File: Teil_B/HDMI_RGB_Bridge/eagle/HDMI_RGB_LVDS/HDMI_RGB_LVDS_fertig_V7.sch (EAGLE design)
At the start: 95 parts, among them CON1 KLDX-0202-A-LT, CON2 FCI-10029449-111RLF, CON3 XF2M-4015-1A, CON4 FCI-10033526-N3212LF, CON5 MOLEX-53261-0671, CON6 FI-X30SSLA-HF, IC2 WPMDL1300331BD, IC4 AT24C01C-SSHM-B, IC5 TFP401APZP, IC6 ATMEGA88PA, IC7 FT232RL, IC8 SN75LVDS83BDGGR, Q1 ATS073ASM-1, T1 IRLML5203TRPBF, T2 IRLML2502TRPBF

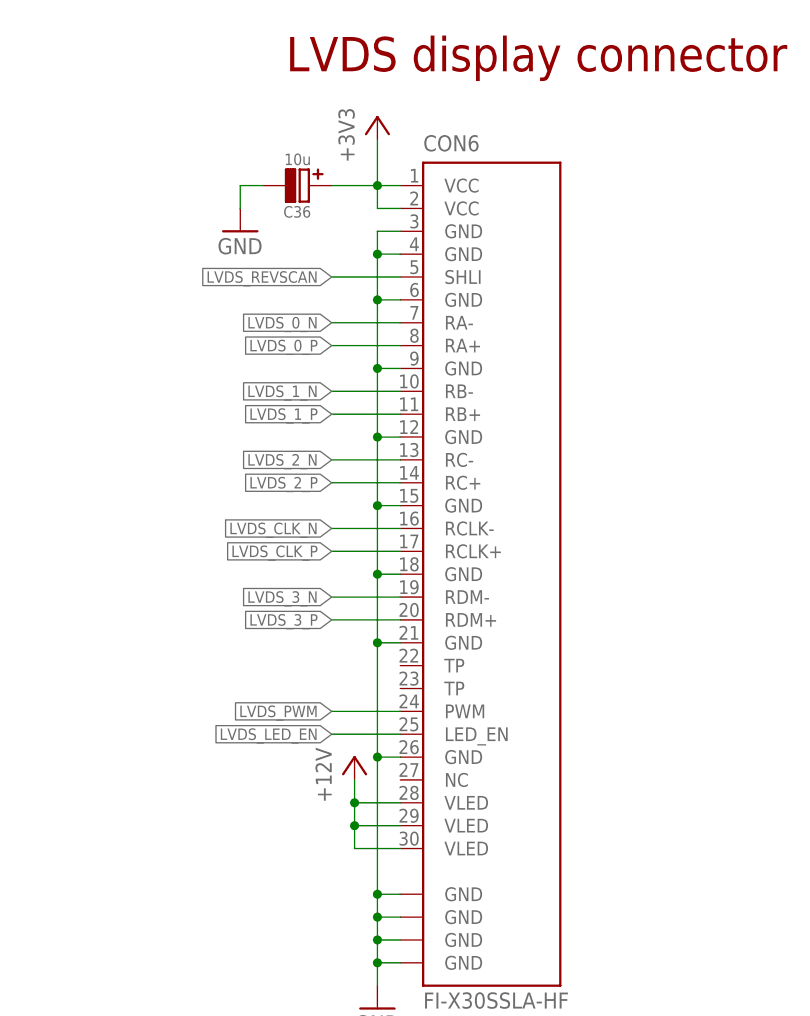
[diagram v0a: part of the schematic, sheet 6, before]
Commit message: reviewd lbr, changd schematics to V7
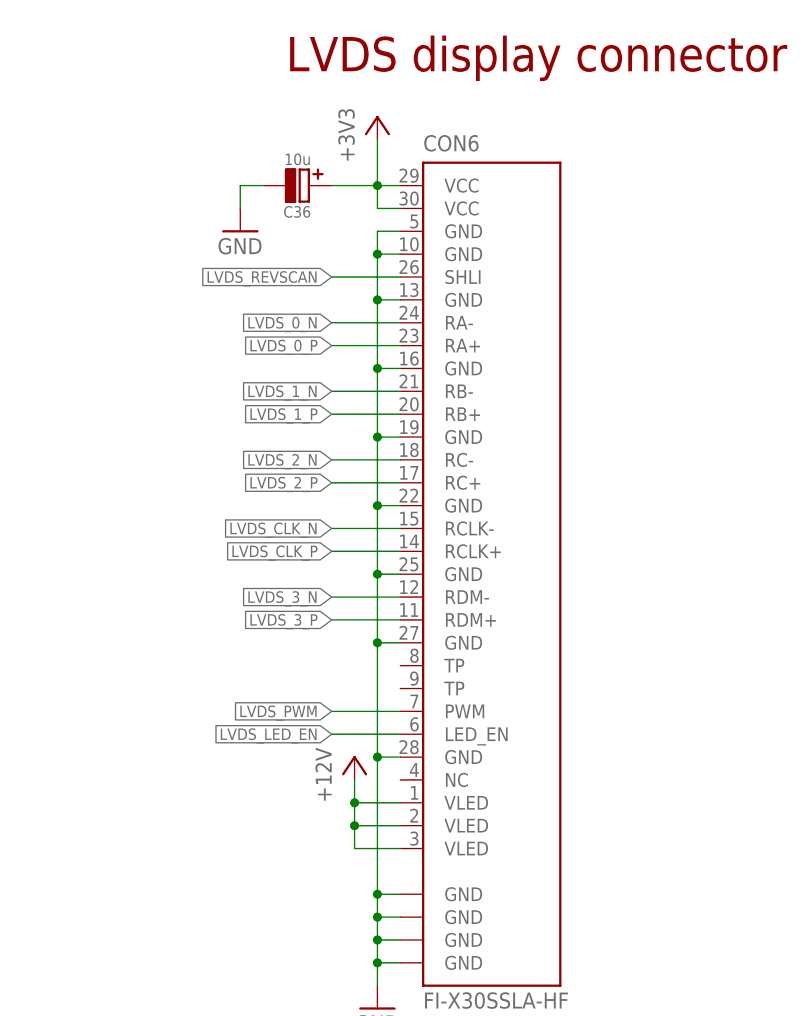
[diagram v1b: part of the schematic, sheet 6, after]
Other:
- note added: "28.04.2014"
- note added: "Layout angepasst, nach Bauteilreview des LVDS Steckers"
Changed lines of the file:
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@@
 <text x="10.16" y="149.86" size="2.54" layer="94">10.04.2014</text>
 <text x="35.56" y="149.86" size="2.54" layer="94">S5: PullUps von I2C auf 4k7 reduziert, Jumper auf I2C Leitungen platziert </text>
+<text x="10.16" y="142.24" size="2.54" layer="94">28.04.2014</text>
+<text x="35.56" y="142.24" size="2.54" layer="94">Layout angepasst, nach Bauteilreview des LVDS Steckers</text>
 </plain>
 <instances>
